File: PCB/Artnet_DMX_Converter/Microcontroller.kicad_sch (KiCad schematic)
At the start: 34 parts, among them J1 Conn_01x03_MountingPin, SW1 SW_Push, SW2 SW_Push, U1 RP2350B, U2 W25Q128JVS, Y1 ABM8-272-T3

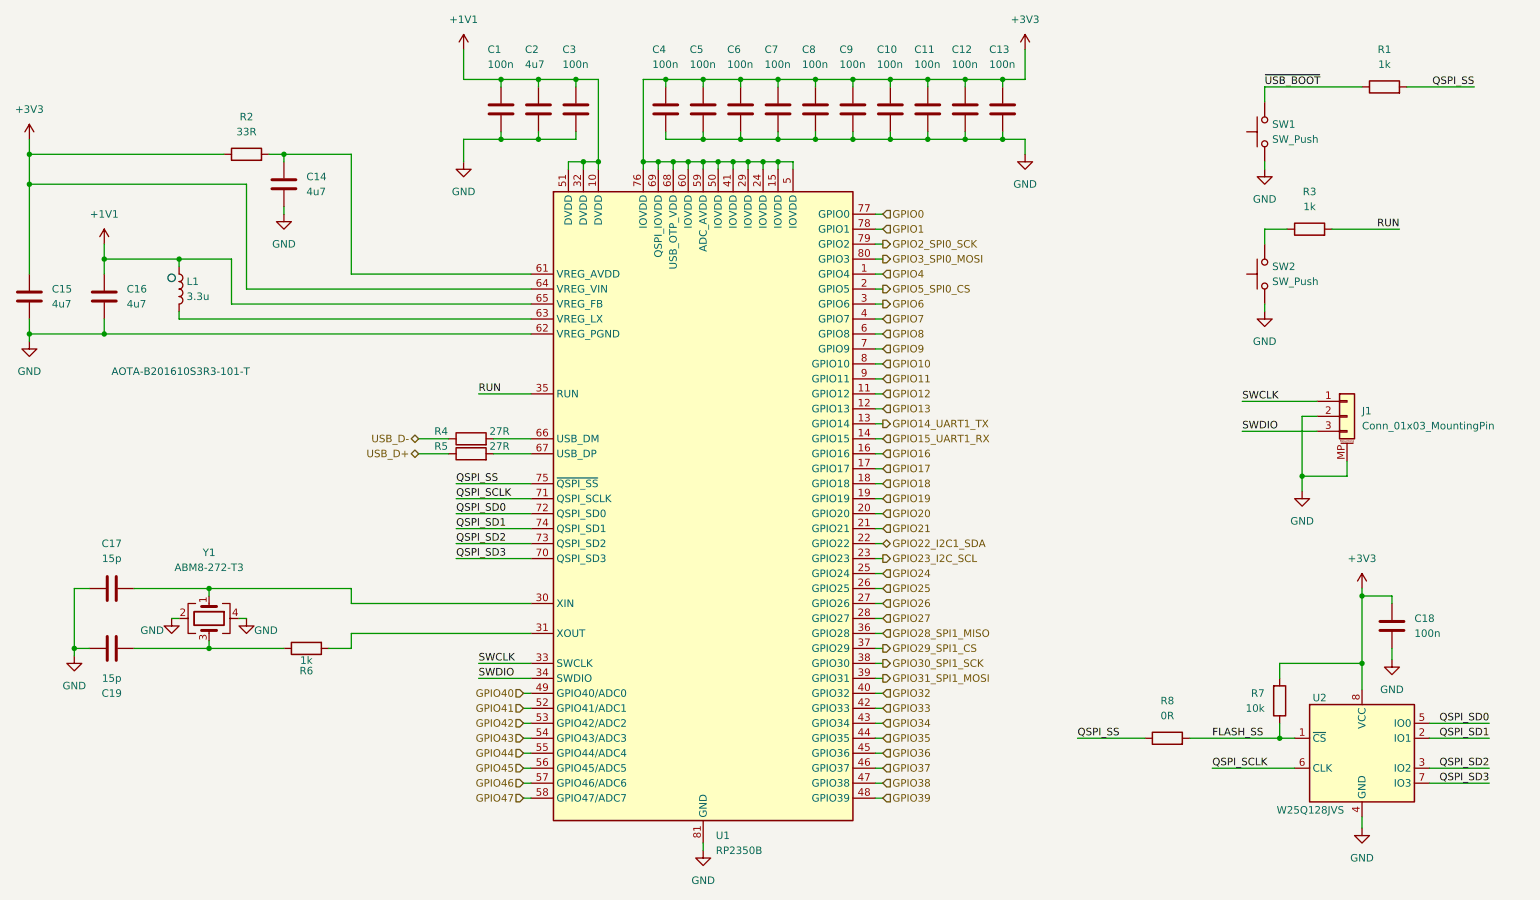
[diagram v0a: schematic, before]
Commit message: Updated the PCB Allot
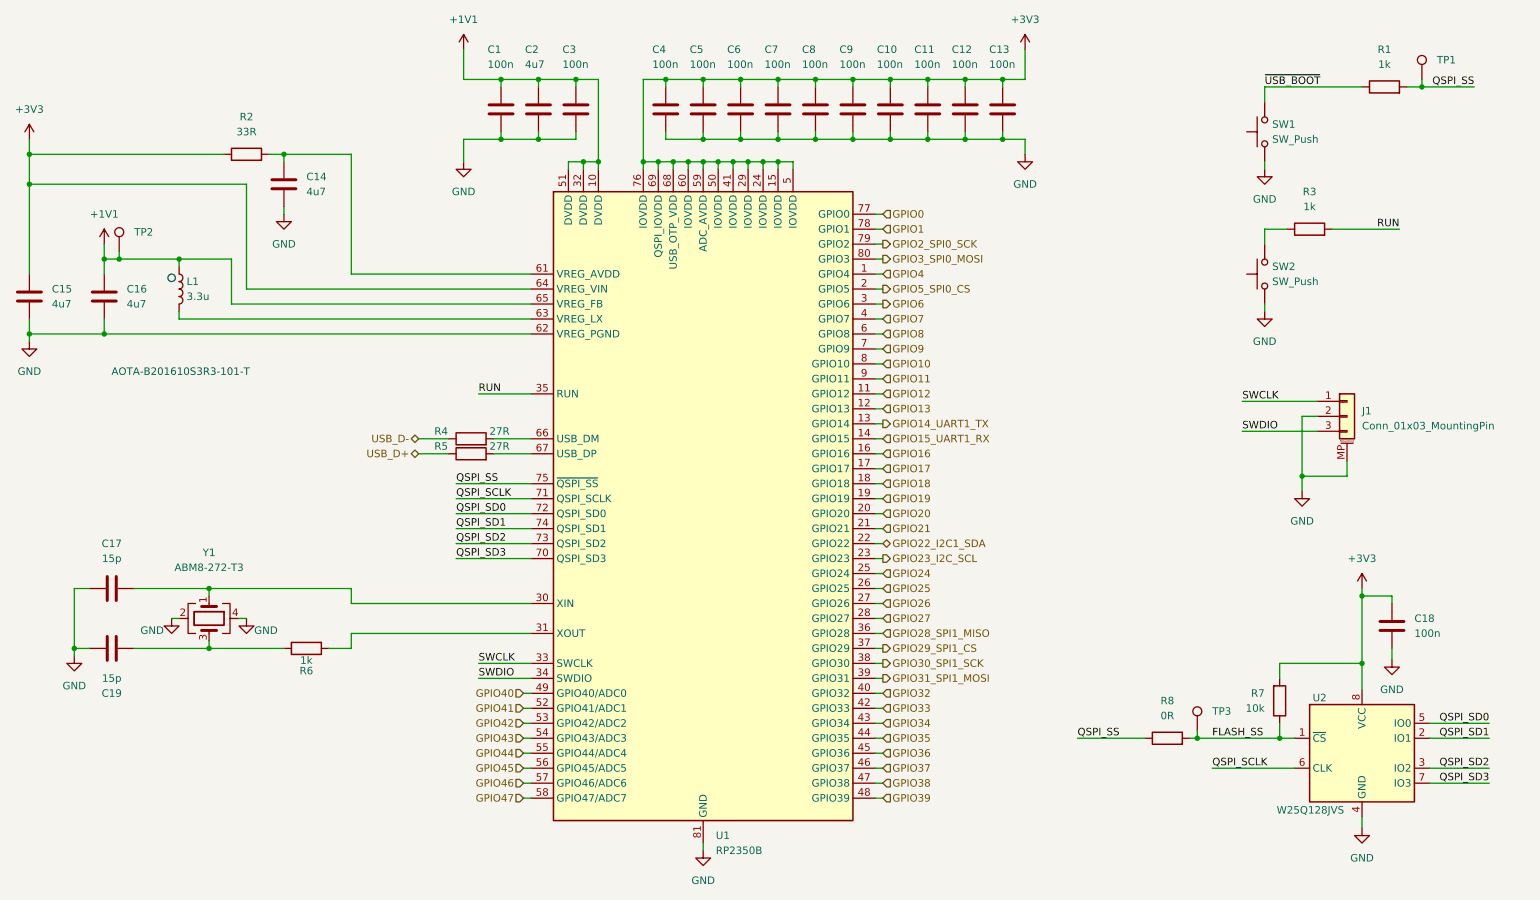
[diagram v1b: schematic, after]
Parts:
- added TP1, TP2, TP3: TestPoint, TestPoint:TestPoint_Pad_D1.5mm, symbol Connector:TestPoint
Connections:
- net +1V1: now also TP2.1
- net FLASH_SS: now also TP3.1
- net QSPI_SS: now also TP1.1
